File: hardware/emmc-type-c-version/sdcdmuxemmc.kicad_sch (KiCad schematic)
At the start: 7 parts, among them J101 USB_C_Receptacle_USB2.0_GCT40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, J102 uSD-CARD-PAD

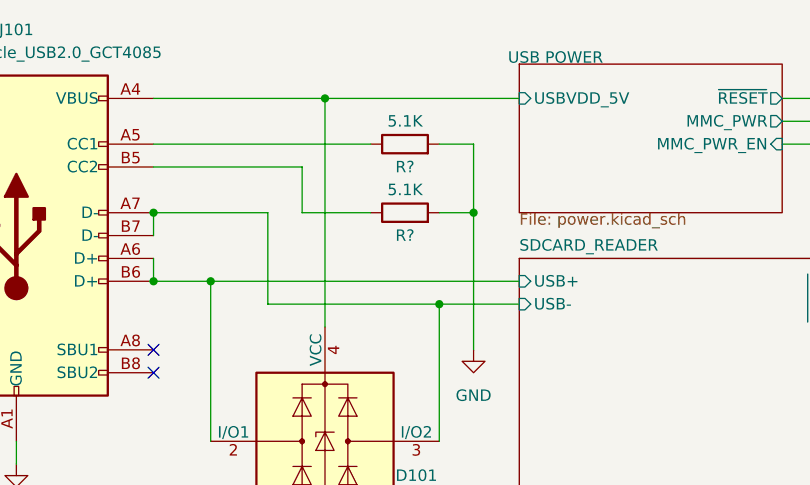
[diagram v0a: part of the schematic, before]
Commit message: Corrected part number in the BOM
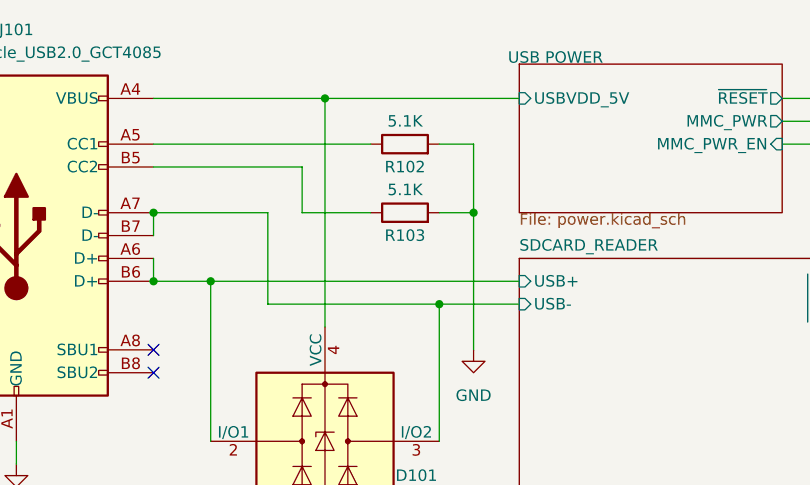
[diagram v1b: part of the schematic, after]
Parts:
- J102: digikey (none) -> Just Pattern
- R101: footprint tbctl:R_0805_2012Metric_Pad1.20x1.40mm_HandSolder -> Resistor_SMD:R_0805_2012Metric_Pad1.20x1.40mm_HandSolder; digikey 13-RC0603JR-1010KLCT-ND -> 311-10KARCT-ND; storeURL https://www.digikey.com/en/products/detail/yageo/RC0603JR-1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 -> https://www.digikey.com/en/products/detail/yageo/RC0805JR-0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
- R102, R103: renamed from R?; footprint tbctl:R_0805_2012Metric_Pad1.20x1.40mm_HandSolder -> Resistor_SMD:R_0805_2012Metric_Pad1.20x1.40mm_HandSolder; digikey 13-RC0603JR-1010KLCT-ND -> 311-5.1KARCT-ND; storeURL https://www.digikey.com/en/products/detail/yageo/RC0603JR-1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 -> https://www.digikey.com/en/products/detail/yageo/RC0805JR-0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
